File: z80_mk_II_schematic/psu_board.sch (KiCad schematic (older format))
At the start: 51 parts

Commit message: Lots more work on schematic
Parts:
- gave numbers to parts that had none: 42
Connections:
- net VBAT renamed VMEM
- net ~EXT_RESET renamed ~EXT_RESET~
- net ~RESET renamed ~RESET~

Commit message: Un-fsck something which made most of the chips into 74LS00 for some very odd reason. Also start to assign footprints.
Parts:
- D10: footprint Diode_THT:D_DO-35_SOD27_P7.62mm_Horizontal -> Diodes_ThroughHole:D_DO-27_P12.70mm_Horizontal
- D4: value D_Small -> 1N4001; footprint (none) -> Diodes_ThroughHole:D_DO-27_P12.70mm_Horizontal
- D5, D6, D7: value D_Small -> 1N4001
- R12, R13, R14, R15, R16, R17, R18, R19, R20, R21: footprint (none) -> Resistors_ThroughHole:R_Axial_DIN0207_L6.3mm_D2.5mm_P10.16mm_Horizontal
- U10: value 74LS04 -> 74LS197; footprint (none) -> Housings_DIP:DIP-14_W7.62mm
- U11: value 74LS04 -> LM555; footprint (none) -> Housings_DIP:DIP-8_W7.62mm
- U6: footprint (none) -> Housings_DIP:DIP-14_W7.62mm_Socket
- U6: renamed from U9; footprint (none) -> Housings_DIP:DIP-14_W7.62mm_Socket
- U7: value 74LS04 -> LM7805; footprint (none) -> TO_SOT_Packages_THT:TO-220-3_Vertical
- U8: value 74LS04 -> 74LS00; footprint (none) -> Housings_DIP:DIP-14_W7.62mm
- Y1: footprint (none) -> Crystals:Crystal_HC49-4H_Vertical
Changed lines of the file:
@@
 P 4050 1750
 F 0 "U7" H 4050 1992 50  0000 C CNN
-F 1 "74LS04" H 4050 1901 50  0000 C CNN
-F 2 "" H 4050 1975 50  0001 C CIN
-F 3 "http://www.ti.com/lit/gpn/sn74LS04" H 4050 1700 50  0001 C CNN
+F 1 "LM7805" H 4050 1901 50  0000 C CNN
+F 2 "TO_SOT_Packages_THT:TO-220-3_Vertical" H 4050 1975 50  0001 C CIN
+F 3 "" H 4050 1700 50  0001 C CNN
 	1    4050 1750
 	1    0    0    -1
@@
 P 2400 1950
 F 0 "D4" V 2354 2020 50  0000 L CNN
-F 1 "D_Small" V 2445 2020 50  0000 L CNN
-F 2 "" V 2400 1950 50  0001 C CNN
+F 1 "1N4001" V 2445 2020 50  0000 L CNN
+F 2 "Diodes_ThroughHole:D_DO-27_P12.70mm_Horizontal" V 2400 1950 50  0001 C CNN
 F 3 "~" V 2400 1950 50  0001 C CNN
 	1    2400 1950
@@
 P 2850 1950
 F 0 "D6" V 2804 2020 50  0000 L CNN
-F 1 "D_Small" V 2895 2020 50  0000 L CNN
+F 1 "1N4001" V 2895 2020 50  0000 L CNN
 F 2 "" V 2850 1950 50  0001 C CNN
 F 3 "~" V 2850 1950 50  0001 C CNN
@@
 P 2850 3100
 F 0 "D7" V 2804 3170 50  0000 L CNN
-F 1 "D_Small" V 2895 3170 50  0000 L CNN
+F 1 "1N4001" V 2895 3170 50  0000 L CNN
 F 2 "" V 2850 3100 50  0001 C CNN
 F 3 "~" V 2850 3100 50  0001 C CNN
@@
 P 2400 3100
 F 0 "D5" V 2354 3170 50  0000 L CNN
-F 1 "D_Small" V 2445 3170 50  0000 L CNN
+F 1 "1N4001" V 2445 3170 50  0000 L CNN
 F 2 "" V 2400 3100 50  0001 C CNN
 F 3 "~" V 2400 3100 50  0001 C CNN
@@
 F 0 "U6" H 4000 4967 50  0000 C CNN
 F 1 "74LS04" H 4000 4876 50  0000 C CNN
-F 2 "" H 4000 4650 50  0001 C CNN
+F 2 "Housings_DIP:DIP-14_W7.62mm_Socket" H 4000 4650 50  0001 C CNN
 F 3 "http://www.ti.com/lit/gpn/sn74LS04" H 4000 4650 50  0001 C CNN
 	1    4000 4650
@@
 F 0 "U6" H 5000 4967 50  0000 C CNN
 F 1 "74LS04" H 5000 4876 50  0000 C CNN
-F 2 "" H 5000 4650 50  0001 C CNN
+F 2 "Housings_DIP:DIP-14_W7.62mm_Socket" H 5000 4650 50  0001 C CNN
 F 3 "http://www.ti.com/lit/gpn/sn74LS04" H 5000 4650 50  0001 C CNN
 	2    5000 4650
@@
 F 0 "R15" V 3804 5050 50  0000 C CNN
 F 1 "1K0" V 3895 5050 50  0000 C CNN
-F 2 "" H 4000 5050 50  0001 C CNN
+F 2 "Resistors_ThroughHole:R_Axial_DIN0207_L6.3mm_D2.5mm_P10.16mm_Horizontal" H 4000 5050 50  0001 C CNN
 F 3 "~" H 4000 5050 50  0001 C CNN
 	1    4000 5050
@@
 F 0 "Y1" H 4450 4418 50  0000 C CNN
 F 1 "4.00MHz" H 4450 4327 50  0000 C CNN
-F 2 "" H 4450 4150 50  0001 C CNN
+F 2 "Crystals:Crystal_HC49-4H_Vertical" H 4450 4150 50  0001 C CNN
 F 3 "~" H 4450 4150 50  0001 C CNN
 	1    4450 4150
@@
 F 0 "R16" V 4804 5050 50  0000 C CNN
 F 1 "1K0" V 4895 5050 50  0000 C CNN
-F 2 "" H 5000 5050 50  0001 C CNN
+F 2 "Resistors_ThroughHole:R_Axial_DIN0207_L6.3mm_D2.5mm_P10.16mm_Horizontal" H 5000 5050 50  0001 C CNN
 F 3 "~" H 5000 5050 50  0001 C CNN
 	1    5000 5050
@@
 F 0 "U6" H 6250 4967 50  0000 C CNN
 F 1 "74LS04" H 6250 4876 50  0000 C CNN
-F 2 "" H 6250 4650 50  0001 C CNN
+F 2 "Housings_DIP:DIP-14_W7.62mm_Socket" H 6250 4650 50  0001 C CNN
 F 3 "http://www.ti.com/lit/gpn/sn74LS04" H 6250 4650 50  0001 C CNN
 	3    6250 4650
@@
 U 1 1 5F9996BA
 P 7500 4350
-F 0 "U10" H 7500 5331 50  0000 C CNN
-F 1 "74LS04" H 7500 5240 50  0000 C CNN
-F 2 "" H 7500 4350 50  0001 C CNN
-F 3 "http://www.ti.com/lit/gpn/sn74LS04" H 7500 4350 50  0001 C CNN
+F 0 "U10" H 7500 4400 50  0000 C CNN
+F 1 "74LS197" H 7550 4250 50  0000 C CNN
+F 2 "Housings_DIP:DIP-14_W7.62mm" H 7500 4350 50  0001 C CNN
+F 3 "" H 7500 4350 50  0001 C CNN
 	1    7500 4350
 	1    0    0    -1
@@
 $Comp
 L 74xx:74LS00 U8
-U 3 1 5F9C4A15
-P 8850 3950
-F 0 "U8" H 8850 4275 50  0000 C CNN
-F 1 "74LS04" H 8850 4184 50  0000 C CNN
-F 2 "" H 8850 3950 50  0001 C CNN
-F 3 "http://www.ti.com/lit/gpn/sn74LS04" H 8850 3950 50  0001 C CNN
-	3    8850 3950
-	1    0    0    -1
-$EndComp
-$Comp
-L 74xx:74LS00 U8
 U 4 1 5F9C8475
 P 8850 4650
 F 0 "U8" H 8850 4975 50  0000 C CNN
-F 1 "74LS04" H 8850 4884 50  0000 C CNN
-F 2 "" H 8850 4650 50  0001 C CNN
-F 3 "http://www.ti.com/lit/gpn/sn74LS04" H 8850 4650 50  0001 C CNN
+F 1 "74LS00" H 8850 4884 50  0000 C CNN
+F 2 "Housings_DIP:DIP-14_W7.62mm" H 8850 4650 50  0001 C CNN
+F 3 "" H 8850 4650 50  0001 C CNN
 	4    8850 4650
 	1    0    0    -1
@@
 P 6500 1750
 F 0 "U8" H 6500 2075 50  0000 C CNN
-F 1 "74LS04" H 6500 1984 50  0000 C CNN
-F 2 "" H 6500 1750 50  0001 C CNN
-F 3 "http://www.ti.com/lit/gpn/sn74LS04" H 6500 1750 50  0001 C CNN
+F 1 "74LS00" H 6500 1984 50  0000 C CNN
+F 2 "Housings_DIP:DIP-14_W7.62mm" H 6500 1750 50  0001 C CNN
+F 3 "" H 6500 1750 50  0001 C CNN
 	1    6500 1750
 	1    0    0    -1
@@
 U 5 1 5F9E1199
 P 4650 6400
-F 0 "U8" H 4880 6446 50  0000 L CNN
-F 1 "74LS04" H 4880 6355 50  0000 L CNN
-F 2 "" H 4650 6400 50  0001 C CNN
-F 3 "http://www.ti.com/lit/gpn/sn74LS04" H 4650 6400 50  0001 C CNN
+F 0 "U8" H 4550 6450 50  0000 L CNN
+F 1 "74LS00" H 4500 6350 50  0000 L CNN
+F 2 "Housings_DIP:DIP-14_W7.62mm" H 4650 6400 50  0001 C CNN
+F 3 "" H 4650 6400 50  0001 C CNN
 	5    4650 6400
 	1    0    0    -1
@@
 F 0 "U6" H 10000 1967 50  0000 C CNN
 F 1 "74LS04" H 10000 1876 50  0000 C CNN
-F 2 "" H 10000 1650 50  0001 C CNN
+F 2 "Housings_DIP:DIP-14_W7.62mm_Socket" H 10000 1650 50  0001 C CNN
 F 3 "http://www.ti.com/lit/gpn/sn74LS04" H 10000 1650 50  0001 C CNN
 	4    10000 1650
@@
 U 1 1 5F99BB6F
 P 8950 1850
-F 0 "U11" H 8950 2431 50  0000 C CNN
-F 1 "74LS04" H 8950 2340 50  0000 C CNN
-F 2 "" H 9600 1450 50  0001 C CNN
-F 3 "http://www.ti.com/lit/gpn/sn74LS04" H 9800 1450 50  0001 C CNN
+F 0 "U11" H 8950 1900 50  0000 C CNN
+F 1 "LM555" H 8950 1800 50  0000 C CNN
+F 2 "Housings_DIP:DIP-8_W7.62mm" H 9600 1450 50  0001 C CNN
+F 3 "" H 9800 1450 50  0001 C CNN
 	1    8950 1850
 	1    0    0    -1
@@
 F 0 "U6" H 7150 1567 50  0000 C CNN
 F 1 "74LS04" H 7150 1476 50  0000 C CNN
-F 2 "" H 7150 1250 50  0001 C CNN
+F 2 "Housings_DIP:DIP-14_W7.62mm_Socket" H 7150 1250 50  0001 C CNN
 F 3 "http://www.ti.com/lit/gpn/sn74LS04" H 7150 1250 50  0001 C CNN
 	5    7150 1250
@@
 F 0 "U6" H 6400 1567 50  0000 C CNN
 F 1 "74LS04" H 6400 1476 50  0000 C CNN
-F 2 "" H 6400 1250 50  0001 C CNN
+F 2 "Housings_DIP:DIP-14_W7.62mm_Socket" H 6400 1250 50  0001 C CNN
 F 3 "http://www.ti.com/lit/gpn/sn74LS04" H 6400 1250 50  0001 C CNN
 	6    6400 1250
@@
 F 0 "D10" H 7850 1467 50  0000 C CNN
 F 1 "1N4148" H 7850 1376 50  0000 C CNN
-F 2 "Diode_THT:D_DO-35_SOD27_P7.62mm_Horizontal" H 7850 1075 50  0001 C CNN
+F 2 "Diodes_ThroughHole:D_DO-27_P12.70mm_Horizontal" H 7850 1075 50  0001 C CNN
 F 3 "https://assets.nexperia.com/documents/data-sheet/1N4148_1N4448.pdf" H 7850 1250 50  0001 C CNN
 	1    7850 1250
@@
 F 0 "R20" V 7854 900 50  0000 C CNN
 F 1 "10K" V 7945 900 50  0000 C CNN
-F 2 "" H 8050 900 50  0001 C CNN
+F 2 "Resistors_ThroughHole:R_Axial_DIN0207_L6.3mm_D2.5mm_P10.16mm_Horizontal" H 8050 900 50  0001 C CNN
 F 3 "~" H 8050 900 50  0001 C CNN
 	1    8050 900
@@
 F 0 "R17" V 5204 950 50  0000 C CNN
 F 1 "100K" V 5295 950 50  0000 C CNN
-F 2 "" H 5400 950 50  0001 C CNN
+F 2 "Resistors_ThroughHole:R_Axial_DIN0207_L6.3mm_D2.5mm_P10.16mm_Horizontal" H 5400 950 50  0001 C CNN
 F 3 "~" H 5400 950 50  0001 C CNN
 	1    5400 950
@@
 F 0 "R21" V 9404 1000 50  0000 C CNN
 F 1 "100K" V 9495 1000 50  0000 C CNN
-F 2 "" H 9600 1000 50  0001 C CNN
+F 2 "Resistors_ThroughHole:R_Axial_DIN0207_L6.3mm_D2.5mm_P10.16mm_Horizontal" H 9600 1000 50  0001 C CNN
 F 3 "~" H 9600 1000 50  0001 C CNN
 	1    9600 1000
@@
 P 7250 1850
 F 0 "U8" H 7250 2175 50  0000 C CNN
-F 1 "74LS04" H 7250 2084 50  0000 C CNN
-F 2 "" H 7250 1850 50  0001 C CNN
-F 3 "http://www.ti.com/lit/gpn/sn74LS04" H 7250 1850 50  0001 C CNN
+F 1 "74LS00" H 7250 2084 50  0000 C CNN
+F 2 "Housings_DIP:DIP-14_W7.62mm" H 7250 1850 50  0001 C CNN
+F 3 "" H 7250 1850 50  0001 C CNN
 	2    7250 1850
 	1    0    0    -1
@@
 F 0 "R18" V 5554 950 50  0000 C CNN
 F 1 "10K" V 5645 950 50  0000 C CNN
-F 2 "" H 5750 950 50  0001 C CNN
+F 2 "Resistors_ThroughHole:R_Axial_DIN0207_L6.3mm_D2.5mm_P10.16mm_Horizontal" H 5750 950 50  0001 C CNN
 F 3 "~" H 5750 950 50  0001 C CNN
 	1    5750 950
@@
 F 0 "R19" V 6504 2200 50  0000 C CNN
 F 1 "10K" V 6595 2200 50  0000 C CNN
-F 2 "" H 6700 2200 50  0001 C CNN
+F 2 "Resistors_ThroughHole:R_Axial_DIN0207_L6.3mm_D2.5mm_P10.16mm_Horizontal" H 6700 2200 50  0001 C CNN
 F 3 "~" H 6700 2200 50  0001 C CNN
 	1    6700 2200
@@
 F 0 "R13" V 2304 5200 50  0000 C CNN
 F 1 "47R" V 2395 5200 50  0000 C CNN
-F 2 "" H 2500 5200 50  0001 C CNN
+F 2 "Resistors_ThroughHole:R_Axial_DIN0207_L6.3mm_D2.5mm_P10.16mm_Horizontal" H 2500 5200 50  0001 C CNN
 F 3 "~" H 2500 5200 50  0001 C CNN
 	1    2500 5200
@@
 F 0 "R12" V 1704 4100 50  0000 C CNN
 F 1 "47R" V 1795 4100 50  0000 C CNN
-F 2 "" H 1900 4100 50  0001 C CNN
+F 2 "Resistors_ThroughHole:R_Axial_DIN0207_L6.3mm_D2.5mm_P10.16mm_Horizontal" H 1900 4100 50  0001 C CNN
 F 3 "~" H 1900 4100 50  0001 C CNN
 	1    1900 4100
@@
 	1200 4800 1200 4650
 $Comp
-L 74xx:74LS00 U9
+L 74xx:74LS00 U6
 U 5 1 5FC902D7
 P 5500 6400
-F 0 "U9" H 5500 6725 50  0000 C CNN
-F 1 "74LS04" H 5500 6634 50  0000 C CNN
-F 2 "" H 5500 6400 50  0001 C CNN
+F 0 "U6" H 5500 6450 50  0000 C CNN
+F 1 "74LS04" H 5500 6350 50  0000 C CNN
+F 2 "Housings_DIP:DIP-14_W7.62mm_Socket" H 5500 6400 50  0001 C CNN
 F 3 "http://www.ti.com/lit/gpn/sn74LS04" H 5500 6400 50  0001 C CNN
 	5    5500 6400
@@
 F 0 "R14" V 3454 6150 50  0000 C CNN
 F 1 "47R" V 3545 6150 50  0000 C CNN
-F 2 "" H 3650 6150 50  0001 C CNN
+F 2 "Resistors_ThroughHole:R_Axial_DIN0207_L6.3mm_D2.5mm_P10.16mm_Horizontal" H 3650 6150 50  0001 C CNN
 F 3 "~" H 3650 6150 50  0001 C CNN
 	1    3650 6150
@@
 	-1   0    0    1
 $EndComp
+$Comp
+L 74xx:74LS00 U8
+U 3 1 5F9C4A15
+P 8850 3950
+F 0 "U8" H 8850 4275 50  0000 C CNN
+F 1 "74LS00" H 8850 4184 50  0000 C CNN
+F 2 "Housings_DIP:DIP-14_W7.62mm" H 8850 3950 50  0001 C CNN
+F 3 "" H 8850 3950 50  0001 C CNN
+	3    8850 3950
+	1    0    0    -1
+$EndComp
 $EndSCHEMATC

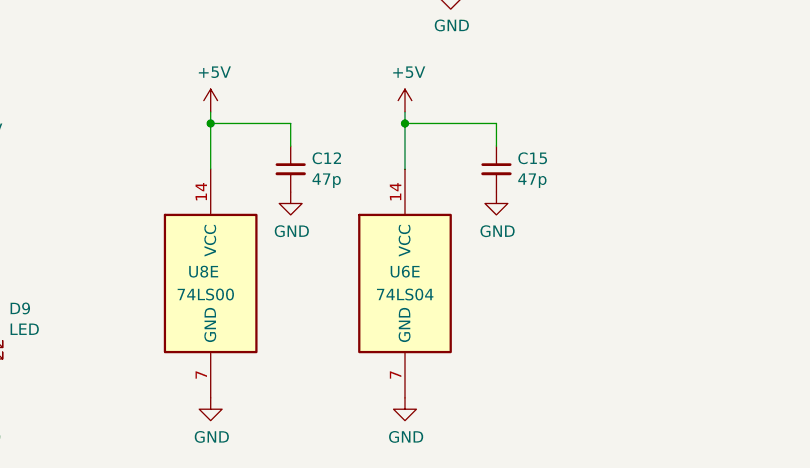
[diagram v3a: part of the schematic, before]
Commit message: Re-annotateand fix doubled-up U6 unit.
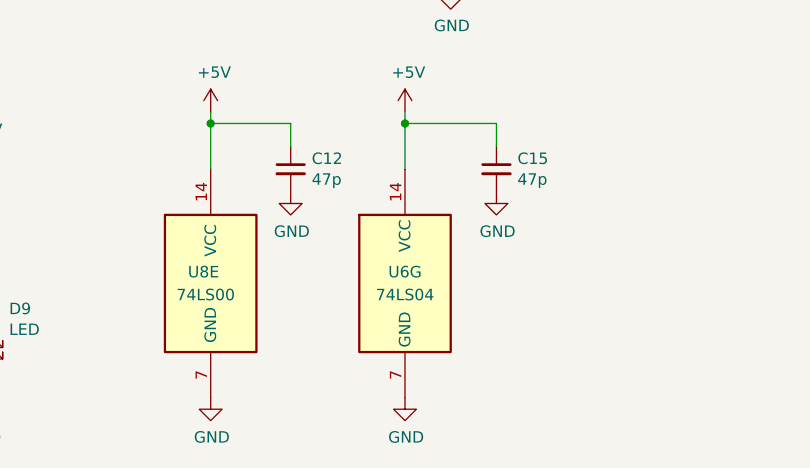
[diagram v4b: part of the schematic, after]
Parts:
- removed U6: 74LS04, Housings_DIP:DIP-14_W7.62mm_Socket, symbol 74xx:74LS00
- added unit 7 of U6
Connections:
- net +5V: now also U6.14 (VCC)
- net GND: now also U6.7 (GND)
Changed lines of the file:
@@
 	1200 4800 1200 4650
-$Comp
-L 74xx:74LS00 U6
-U 5 1 5FC902D7
-P 5500 6400
-F 0 "U6" H 5500 6450 50  0000 C CNN
-F 1 "74LS04" H 5500 6350 50  0000 C CNN
-F 2 "Housings_DIP:DIP-14_W7.62mm_Socket" H 5500 6400 50  0001 C CNN
-F 3 "http://www.ti.com/lit/gpn/sn74LS04" H 5500 6400 50  0001 C CNN
-	5    5500 6400
-	1    0    0    -1
-$EndComp
 $Comp
 L power:GND #PWR040
@@
 	1    0    0    -1
 $EndComp
+$Comp
+L 74xx:74LS04 U6
+U 7 1 5FA114BB
+P 5500 6400
+F 0 "U6" H 5500 6450 50  0000 C CNN
+F 1 "74LS04" H 5500 6350 50  0000 C CNN
+F 2 "Housings_DIP:DIP-14_W7.62mm_Socket" H 5500 6400 50  0001 C CNN
+F 3 "http://www.ti.com/lit/gpn/sn74LS04" H 5500 6400 50  0001 C CNN
+	7    5500 6400
+	1    0    0    -1
+$EndComp

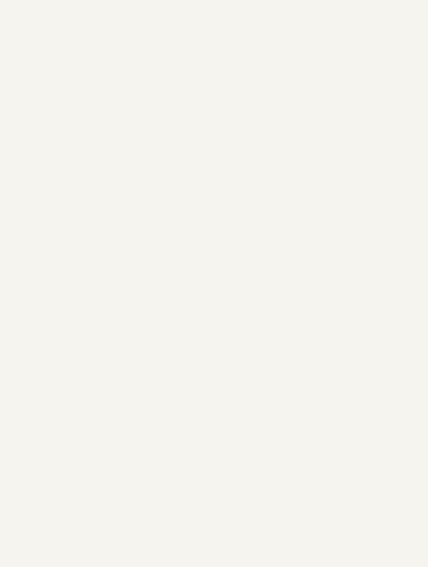
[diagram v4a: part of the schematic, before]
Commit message: Add some no-connection symbols.
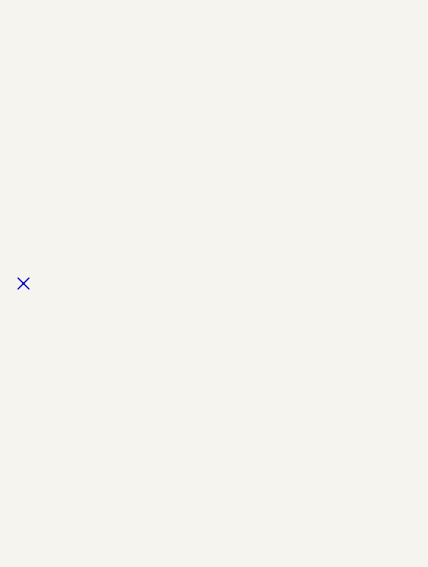
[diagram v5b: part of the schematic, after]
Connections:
- no-connect marks 0 -> 1
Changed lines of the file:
@@
 	1    0    0    -1
 $EndComp
+NoConn ~ -9250 3300
 $EndSCHEMATC
